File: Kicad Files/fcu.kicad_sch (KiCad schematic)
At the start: 23 parts, among them J10 EXPED, J11 APPR, J30 SPD/MACH, J31 HDG/TRK, J32 MET_ALT, J33 LVL_OFF, J34 SPD_ENC, J35 HDG_ENC, J36 A_PULL, J36 A_PUSH, J41 S_PULL, J41 S_PUSH, J43 H_PULL, J43 H_PUSH, J44 ALT_ENC, J45 A_1H_1K, J46 VS_PULL, J46 VS_PUSH, J48 VS_ENC, J6 AP1, J7 AP2, J8 A/THR, J9 LOC

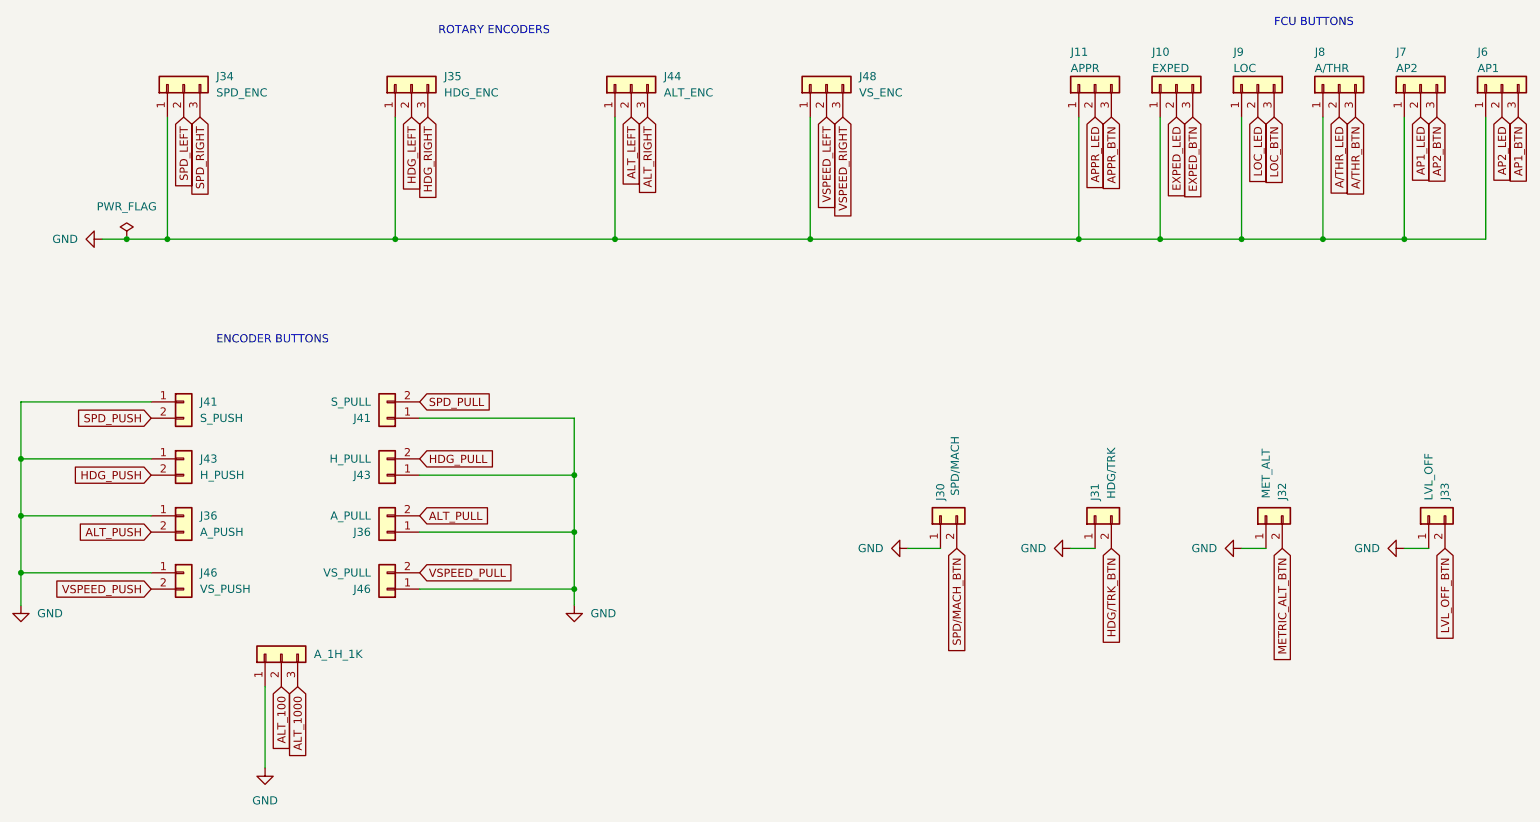
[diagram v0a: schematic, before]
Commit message: Complete rework of panels to be printed facedown. Important: change the order of the colors as Grey, White, Black, Transparent if using a Bambulab P1S/X1C ALso corrected some issue with the PCB (optional, you can print the FCU without using my pcb)
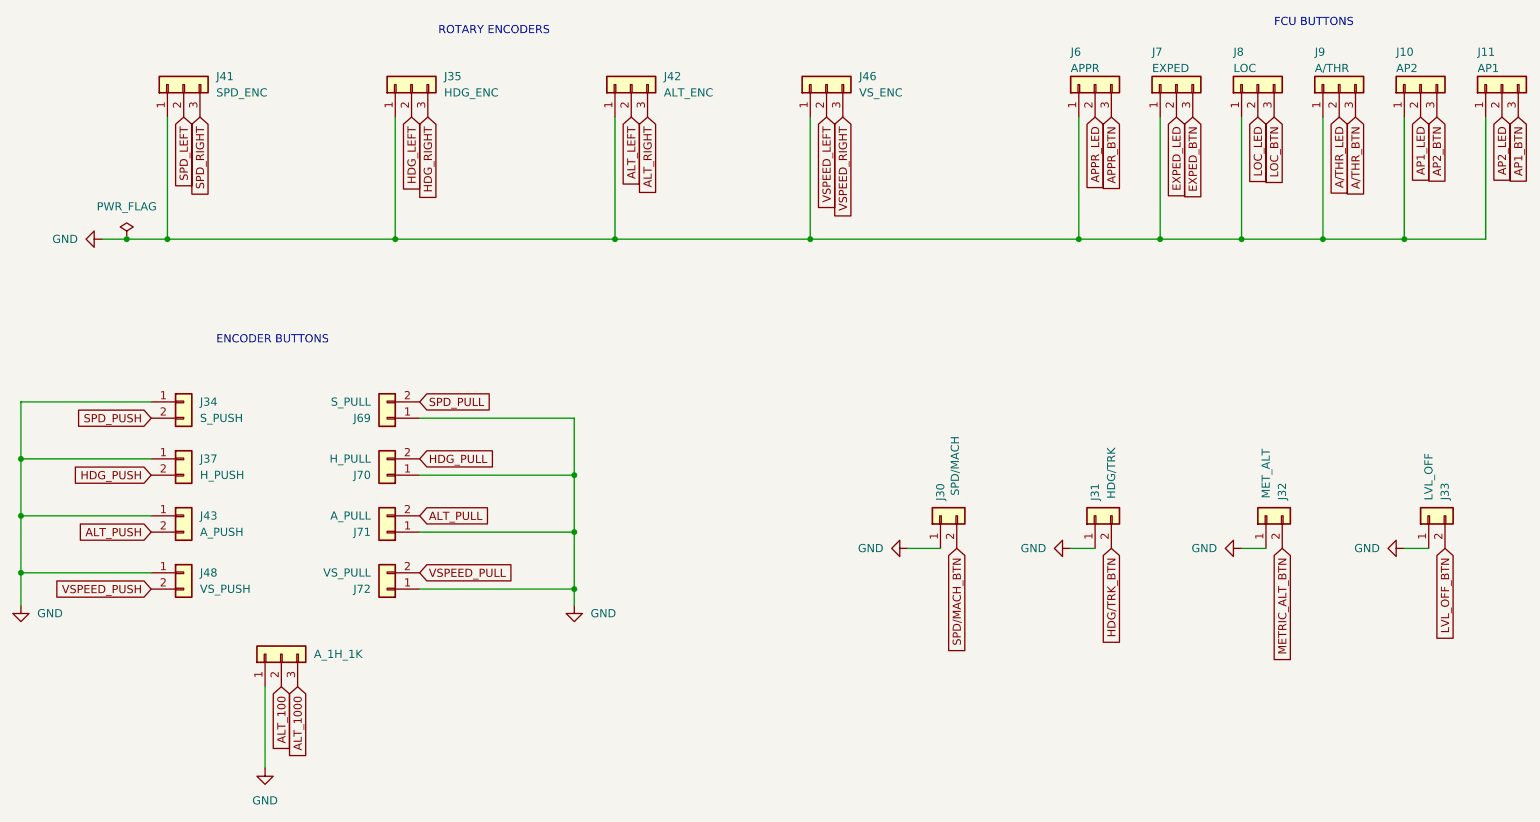
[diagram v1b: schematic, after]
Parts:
- renumbered J7 to J10, J6 to J11, J41 to J34, J43 to J37, J34 to J41, J44 to J42, J36 to J43, J48 to J46, J46 to J48, J11 to J6, J41 to J69, J10 to J7, J43 to J70, J36 to J71, J46 to J72, J9 to J8, J8 to J9
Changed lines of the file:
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@@
 (kicad_sch
-	(version 20231120)
+	(version 20250114)
 	(generator "eeschema")
-	(generator_version "8.0")
+	(generator_version "9.0")
 	(paper "A4")
 	(title_block
@@
 		(rev "1.0")
 	)
+	(text "ROTARY ENCODERS"
+		(exclude_from_sim no)
+		(at 107.95 27.94 0)
+		(effects
+			(font
+				(size 1.27 1.27)
+			)
+			(justify right bottom)
+		)
+	)
+	(text "ENCODER BUTTONS"
+		(exclude_from_sim no)
+		(at 55.88 76.2 0)
+		(effects
+			(font
+				(size 1.27 1.27)
+			)
+			(justify left bottom)
+		)
+	)
+	(text "FCU BUTTONS"
+		(exclude_from_sim no)
+		(at 220.98 26.67 0)
+		(effects
+			(font
+				(size 1.27 1.27)
+			)
+			(justify left bottom)
+		)
+	)
 	(junction
 		(at 228.6 59.69)
@@
 		)
 	)
-	(text "ROTARY ENCODERS"
-		(exclude_from_sim no)
-		(at 107.95 27.94 0)
-		(effects
-			(font
-				(size 1.27 1.27)
-			)
-			(justify right bottom)
-		)
-	)
-	(text "ENCODER BUTTONS"
-		(exclude_from_sim no)
-		(at 55.88 76.2 0)
-		(effects
-			(font
-				(size 1.27 1.27)
-			)
-			(justify left bottom)
-		)
-	)
-	(text "FCU BUTTONS"
-		(exclude_from_sim no)
-		(at 220.98 26.67 0)
-		(effects
-			(font
-				(size 1.27 1.27)
-			)
-			(justify left bottom)
-		)
-	)
 	(global_label "ALT_PULL"
 		(shape input)
@@
 		(dnp no)
 		(fields_autoplaced yes)
-		(property "Reference" "J48"
+		(property "Reference" "J46"
 			(at 156.21 34.2899 90)
 			(effects
@@
 		(on_board yes)
 		(dnp no)
-		(property "Reference" "J9"
+		(property "Reference" "J8"
 			(at 214.63 30.48 90)
 			(effects
@@
 		(dnp no)
 		(fields_autoplaced yes)
-		(property "Reference" "J34"
+		(property "Reference" "J41"
 			(at 55.88 34.2899 90)
 			(effects
@@
 		(on_board yes)
 		(dnp no)
-		(property "Reference" "J8"
+		(property "Reference" "J9"
 			(at 227.33 30.48 90)
 			(effects
@@
 		(on_board yes)
 		(dnp no)
-		(property "Reference" "J36"
+		(property "Reference" "J71"
 			(at 80.01 105.41 0)
 			(do_not_autoplace yes)
@@
 		(on_board yes)
 		(dnp no)
-		(property "Reference" "J11"
+		(property "Reference" "J6"
 			(at 189.23 30.48 90)
 			(effects
@@
 		(dnp no)
 		(fields_autoplaced yes)
-		(property "Reference" "J46"
+		(property "Reference" "J48"
 			(at 53.34 111.7599 0)
 			(effects
@@
 		(on_board yes)
 		(dnp no)
-		(property "Reference" "J6"
+		(property "Reference" "J11"
 			(at 252.73 30.48 90)
 			(effects
@@
 		(on_board yes)
 		(dnp no)
-		(property "Reference" "J46"
+		(property "Reference" "J72"
 			(at 80.01 114.3 0)
 			(do_not_autoplace yes)
@@
 		(dnp no)
 		(fields_autoplaced yes)
-		(property "Reference" "J36"
+		(property "Reference" "J43"
 			(at 53.34 102.8699 0)
 			(effects
@@
 		(on_board yes)
 		(dnp no)
-		(property "Reference" "J41"
+		(property "Reference" "J69"
 			(at 80.01 87.63 0)
 			(do_not_autoplace yes)
@@
 		(dnp no)
 		(fields_autoplaced yes)
-		(property "Reference" "J43"
+		(property "Reference" "J37"
 			(at 53.34 93.9799 0)
 			(effects
@@
 		(on_board yes)
 		(dnp no)
-		(property "Reference" "J10"
+		(property "Reference" "J7"
 			(at 201.93 30.48 90)
 			(effects
@@
 		(on_board yes)
 		(dnp no)
-		(property "Reference" "J7"
+		(property "Reference" "J10"
 			(at 240.03 30.48 90)
 			(effects
@@
 		(on_board yes)
 		(dnp no)
-		(property "Reference" "J43"
+		(property "Reference" "J70"
 			(at 80.01 96.52 0)
 			(do_not_autoplace yes)
@@
 		(dnp no)
 		(fields_autoplaced yes)
-		(property "Reference" "J41"
+		(property "Reference" "J34"
 			(at 53.34 85.0899 0)
 			(effects
@@
 		(dnp no)
 		(fields_autoplaced yes)
-		(property "Reference" "J44"
+		(property "Reference" "J42"
 			(at 125.73 34.2899 90)
 			(effects
